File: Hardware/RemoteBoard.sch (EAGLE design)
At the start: 37 parts, among them J1 SOCKETS9111_SLOT, J2 SOCKETS9111_SLOT, J3 SOCKETS9111_SLOT, J4 CONN_42.54_SCREW, Q3 DMG3404, U1 SPG30, U2 TXS0102DCU, U3 MIC53651.8SC70, U4 BME280, U5 LTC2054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

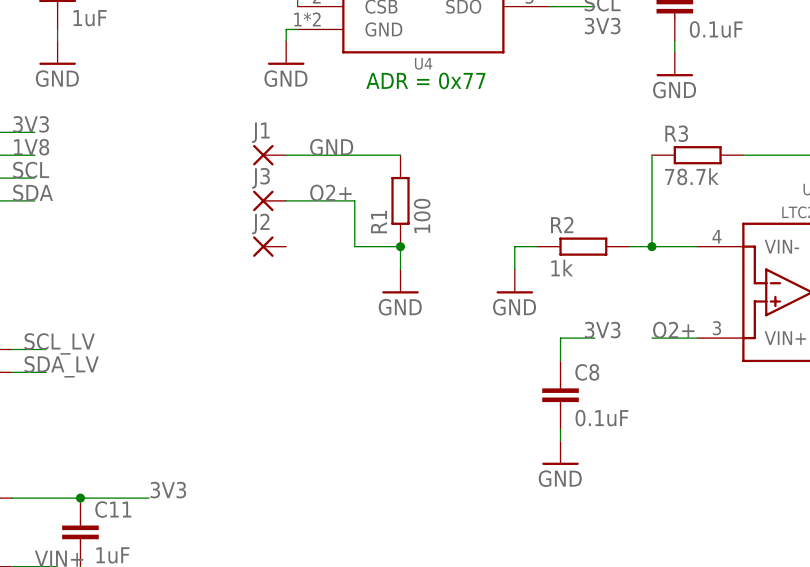
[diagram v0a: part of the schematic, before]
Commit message: Removed erroneous GND symbol
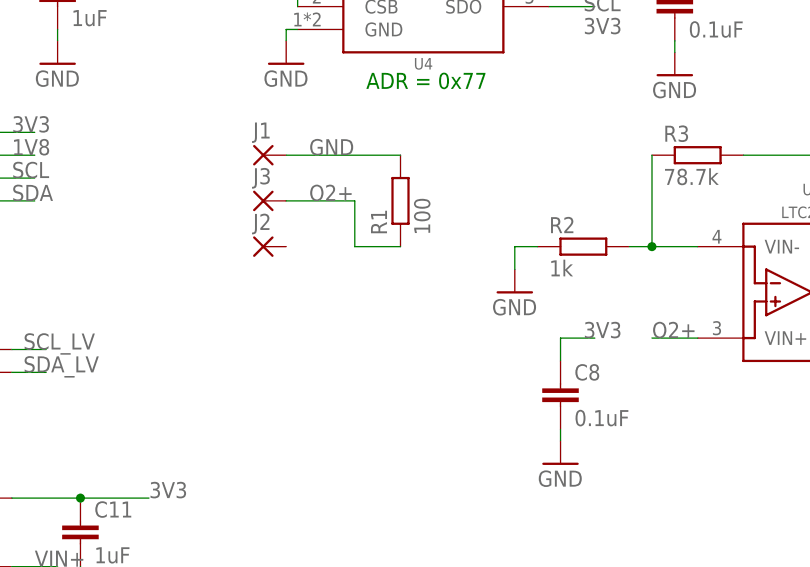
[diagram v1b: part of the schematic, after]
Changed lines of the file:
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@@
 <setting verticaltext="up"/>
 </settings>
-<grid distance="0.1" unitdist="inch" unit="mm" style="lines" multiple="1" display="no" altdistance="0.01" altunitdist="inch" altunit="mm"/>
+<grid distance="0.1" unitdist="inch" unit="inch" style="lines" multiple="1" display="no" altdistance="0.01" altunitdist="inch" altunit="inch"/>
 <layers>
-<layer number="1" name="Top" color="4" fill="1" visible="yes" active="no"/>
-<layer number="2" name="Route2" color="16" fill="1" visible="yes" active="no"/>
-<layer number="3" name="Route3" color="17" fill="1" visible="yes" active="no"/>
-<layer number="4" name="Route4" color="18" fill="1" visible="yes" active="no"/>
-<layer number="5" name="Route5" color="19" fill="1" visible="yes" active="no"/>
-<layer number="6" name="Route6" color="25" fill="1" visible="yes" active="no"/>
-<layer number="7" name="Route7" color="26" fill="1" visible="yes" active="no"/>
-<layer number="8" name="Route8" color="27" fill="1" visible="yes" active="no"/>
-<layer number="9" name="Route9" color="28" fill="1" visible="yes" active="no"/>
-<layer number="10" name="Route10" color="29" fill="1" visible="yes" active="no"/>
-<layer number="11" name="Route11" color="30" fill="1" visible="yes" active="no"/>
-<layer number="12" name="Route12" color="20" fill="1" visible="yes" active="no"/>
-<layer number="13" name="Route13" color="21" fill="1" visible="yes" active="no"/>
-<layer number="14" name="Route14" color="22" fill="1" visible="yes" active="no"/>
-<layer number="15" name="Route15" color="23" fill="1" visible="yes" active="no"/>
-<layer number="16" name="Bottom" color="1" fill="1" visible="yes" active="no"/>
-<layer number="17" name="Pads" color="2" fill="1" visible="yes" active="no"/>
-<layer number="18" name="Vias" color="2" fill="1" visible="yes" active="no"/>
-<layer number="19" name="Unrouted" color="6" fill="1" visible="yes" active="no"/>
-<layer number="20" name="Dimension" color="24" fill="1" visible="yes" active="no"/>
-<layer number="21" name="tPlace" color="7" fill="1" visible="yes" active="no"/>
-<layer number="22" name="bPlace" color="7" fill="1" visible="yes" active="no"/>
-<layer number="23" name="tOrigins" color="15" fill="1" visible="yes" active="no"/>
-<layer number="24" name="bOrigins" color="15" fill="1" visible="yes" active="no"/>
-<layer number="25" name="tNames" color="7" fill="1" visible="yes" active="no"/>
-<layer number="26" name="bNames" color="7" fill="1" visible="yes" active="no"/>
-<layer number="27" name="tValues" color="7" fill="1" visible="yes" active="no"/>
-<layer number="28" name="bValues" color="7" fill="1" visible="yes" active="no"/>
+<layer number="1" name="Top" color="4" fill="1" visible="no" active="no"/>
+<layer number="2" name="Route2" color="16" fill="1" visible="no" active="no"/>
+<layer number="3" name="Route3" color="17" fill="1" visible="no" active="no"/>
+<layer number="4" name="Route4" color="18" fill="1" visible="no" active="no"/>
+<layer number="5" name="Route5" color="19" fill="1" visible="no" active="no"/>
+<layer number="6" name="Route6" color="25" fill="1" visible="no" active="no"/>
+<layer number="7" name="Route7" color="26" fill="1" visible="no" active="no"/>
+<layer number="8" name="Route8" color="27" fill="1" visible="no" active="no"/>
+<layer number="9" name="Route9" color="28" fill="1" visible="no" active="no"/>
+<layer number="10" name="Route10" color="29" fill="1" visible="no" active="no"/>
+<layer number="11" name="Route11" color="30" fill="1" visible="no" active="no"/>
+<layer number="12" name="Route12" color="20" fill="1" visible="no" active="no"/>
+<layer number="13" name="Route13" color="21" fill="1" visible="no" active="no"/>
+<layer number="14" name="Route14" color="22" fill="1" visible="no" active="no"/>
+<layer number="15" name="Route15" color="23" fill="1" visible="no" active="no"/>
+<layer number="16" name="Bottom" color="1" fill="1" visible="no" active="no"/>
+<layer number="17" name="Pads" color="2" fill="1" visible="no" active="no"/>
+<layer number="18" name="Vias" color="2" fill="1" visible="no" active="no"/>
+<layer number="19" name="Unrouted" color="6" fill="1" visible="no" active="no"/>
+<layer number="20" name="Dimension" color="24" fill="1" visible="no" active="no"/>
+<layer number="21" name="tPlace" color="7" fill="1" visible="no" active="no"/>
+<layer number="22" name="bPlace" color="7" fill="1" visible="no" active="no"/>
+<layer number="23" name="tOrigins" color="15" fill="1" visible="no" active="no"/>
+<layer number="24" name="bOrigins" color="15" fill="1" visible="no" active="no"/>
+<layer number="25" name="tNames" color="7" fill="1" visible="no" active="no"/>
+<layer number="26" name="bNames" color="7" fill="1" visible="no" active="no"/>
+<layer number="27" name="tValues" color="7" fill="1" visible="no" active="no"/>
+<layer number="28" name="bValues" color="7" fill="1" visible="no" active="no"/>
 <layer number="29" name="tStop" color="7" fill="3" visible="no" active="no"/>
 <layer number="30" name="bStop" color="7" fill="6" visible="no" active="no"/>
@@
 <layer number="35" name="tGlue" color="7" fill="4" visible="no" active="no"/>
 <layer number="36" name="bGlue" color="7" fill="5" visible="no" active="no"/>
-<layer number="37" name="tTest" color="7" fill="1" visible="yes" active="no"/>
-<layer number="38" name="bTest" color="7" fill="1" visible="yes" active="no"/>
+<layer number="37" name="tTest" color="7" fill="1" visible="no" active="no"/>
+<layer number="38" name="bTest" color="7" fill="1" visible="no" active="no"/>
 <layer number="39" name="tKeepout" color="4" fill="11" visible="no" active="no"/>
 <layer number="40" name="bKeepout" color="1" fill="11" visible="no" active="no"/>
@@
 <layer number="44" name="Drills" color="7" fill="1" visible="no" active="no"/>
 <layer number="45" name="Holes" color="7" fill="1" visible="no" active="no"/>
-<layer number="46" name="Milling" color="3" fill="1" visible="yes" active="no"/>
-<layer number="47" name="Measures" color="7" fill="1" visible="yes" active="no"/>
-<layer number="48" name="Document" color="7" fill="1" visible="yes" active="no"/>
-<layer number="49" name="Reference" color="7" fill="1" visible="yes" active="no"/>
-<layer number="50" name="dxf" color="7" fill="1" visible="yes" active="no"/>
-<layer number="51" name="tDocu" color="7" fill="1" visible="yes" active="no"/>
-<layer number="52" name="bDocu" color="7" fill="1" visible="yes" active="no"/>
-<layer number="53" name="tGND_GNDA" color="7" fill="1" visible="yes" active="no"/>
-<layer number="54" name="bGND_GNDA" color="7" fill="1" visible="yes" active="no"/>
-<layer number="56" name="wert" color="7" fill="1" visible="yes" active="no"/>
-<layer number="57" name="tCAD" color="7" fill="1" visible="yes" active="no"/>
-<layer number="59" name="tCarbon" color="7" fill="1" visible="yes" active="no"/>
-<layer number="60" name="bCarbon" color="7" fill="1" visible="yes" active="no"/>
+<layer number="46" name="Milling" color="3" fill="1" visible="no" active="no"/>
+<layer number="47" name="Measures" color="7" fill="1" visible="no" active="no"/>
+<layer number="48" name="Document" color="7" fill="1" visible="no" active="no"/>
+<layer number="49" name="Reference" color="7" fill="1" visible="no" active="no"/>
+<layer number="50" name="dxf" color="7" fill="1" visible="no" active="no"/>
+<layer number="51" name="tDocu" color="7" fill="1" visible="no" active="no"/>
+<layer number="52" name="bDocu" color="7" fill="1" visible="no" active="no"/>
+<layer number="53" name="tGND_GNDA" color="7" fill="1" visible="no" active="no"/>
+<layer number="54" name="bGND_GNDA" color="7" fill="1" visible="no" active="no"/>
+<layer number="56" name="wert" color="7" fill="1" visible="no" active="no"/>
+<layer number="57" name="tCAD" color="7" fill="1" visible="no" active="no"/>
+<layer number="59" name="tCarbon" color="7" fill="1" visible="no" active="no"/>
+<layer number="60" name="bCarbon" color="7" fill="1" visible="no" active="no"/>
 <layer number="88" name="SimResults" color="9" fill="1" visible="yes" active="yes"/>
 <layer number="89" name="SimProbes" color="9" fill="1" visible="yes" active="yes"/>
@@
 <part name="U5" library="bschulz" deviceset="LTC2054" device=""/>
 <part name="R1" library="bschulz_passives" deviceset="R-EU_" device="R0805" technology="100" value="100"/>
-<part name="GND8" library="supply1" library_urn="urn:adsk.eagle:library:371" deviceset="GND" device=""/>
 <part name="R2" library="bschulz_passives" deviceset="R-EU_" device="R0805" technology="1K" value="1k"/>
 <part name="R3" library="bschulz_passives" deviceset="R-EU_" device="R0805" technology="78.7K" value="78.7k"/>
@@
 <attribute name="VALUE" x="104.902" y="36.83" size="1.778" layer="96" rot="R90"/>
 </instance>
-<instance part="GND8" gate="1" x="101.6" y="30.48" smashed="yes">
-<attribute name="VALUE" x="99.06" y="27.94" size="1.778" layer="96"/>
-</instance>
 <instance part="R2" gate="G$1" x="121.92" y="35.56" smashed="yes">
 <attribute name="NAME" x="118.11" y="37.0586" size="1.778" layer="95"/>
@@
 <pinref part="R1" gate="G$1" pin="1"/>
 <wire x1="96.52" y1="35.56" x2="101.6" y2="35.56" width="0.1524" layer="91"/>
-<pinref part="GND8" gate="1" pin="GND"/>
-<wire x1="101.6" y1="33.02" x2="101.6" y2="35.56" width="0.1524" layer="91"/>
-<junction x="101.6" y="35.56"/>
 </segment>
 </net>
